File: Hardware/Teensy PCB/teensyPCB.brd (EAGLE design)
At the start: 100 x 50 mm, 9 parts, among them U1 HC_05, U2 USD-SOCKETNEW

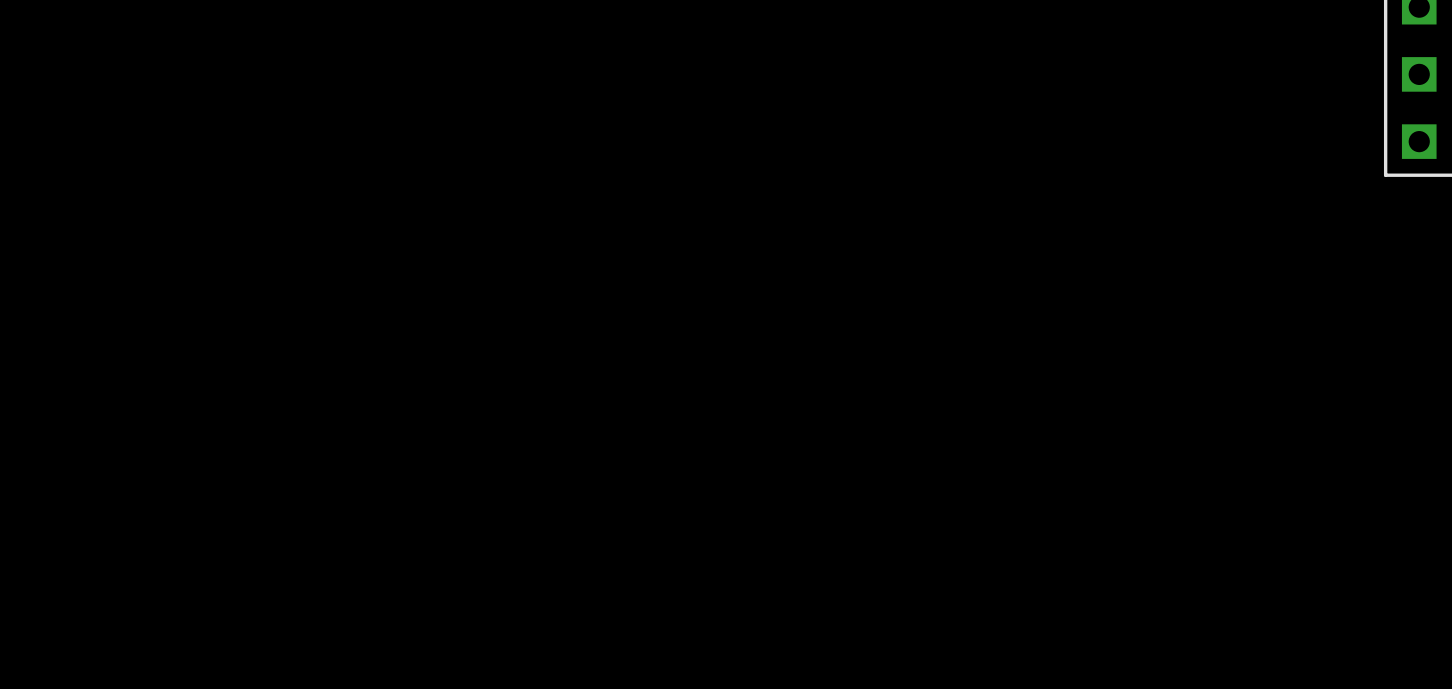
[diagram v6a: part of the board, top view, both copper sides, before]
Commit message: First attempt at wiring the audio (could be totally wrong)
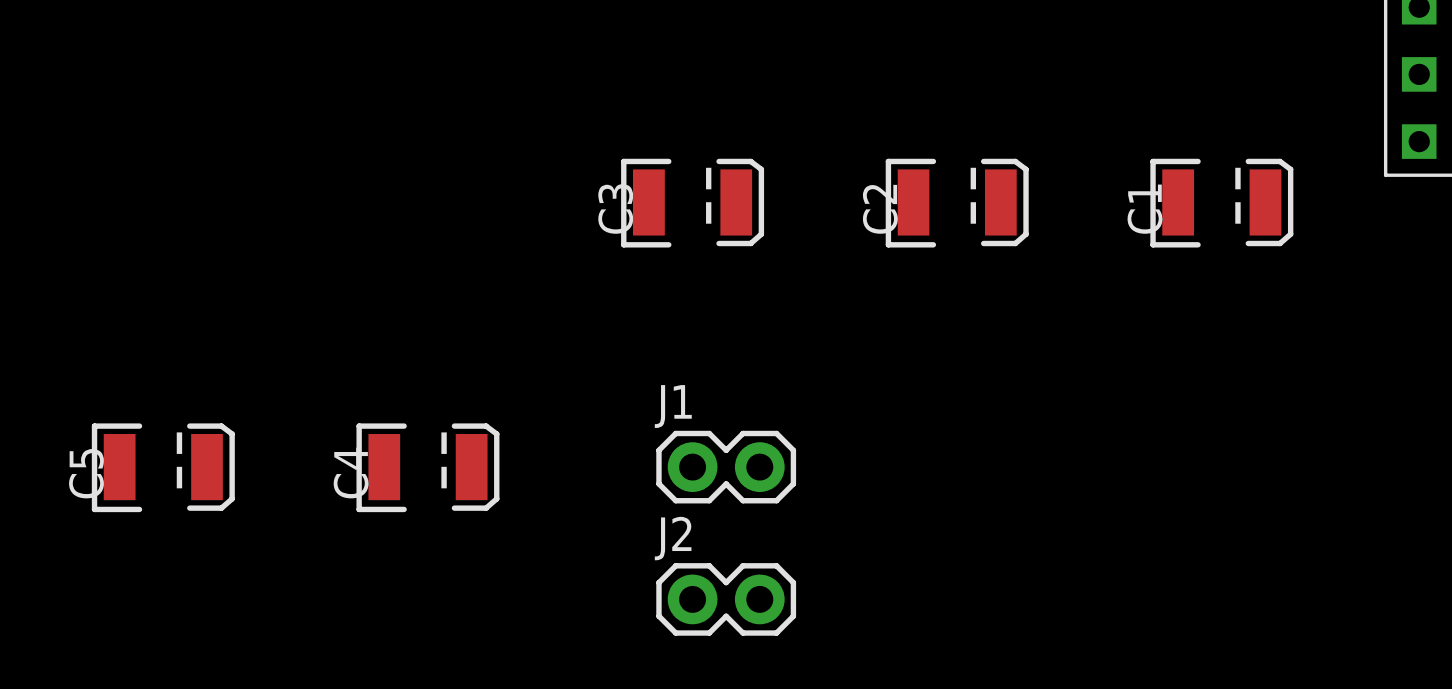
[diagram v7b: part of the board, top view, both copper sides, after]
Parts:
- added C1: 47uF, SparkFun-Capacitors:EIA3528
- added C2, C3: 10uF, SparkFun-Capacitors:EIA3528
- added C4, C5: 470uF, SparkFun-Capacitors:EIA3528
- added J1, J2: (no value), SparkFun-Connectors:1X02
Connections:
- new net DAC: C2.A, C3.A, U$1.RESET/DAC
- new net N$1: C2.C, U$4.LN
- new net N$2: C3.C, U$4.RN
- new net N$3: C4.C, J1.2
- new net N$4: C5.C, J2.2
- new net N$5: C4.A, U$4.R+
- new net N$6: J1.1, U$4.R-
- new net N$7: J2.1, U$4.L-
- new net N$8: C5.A, U$4.L+
- net 5V: now also C1.A
- net GND: now also C1.C
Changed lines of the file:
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@@
 <layer number="56" name="wert" color="7" fill="1" visible="yes" active="yes"/>
 <layer number="57" name="tCAD" color="7" fill="1" visible="no" active="no"/>
+<layer number="59" name="tCarbon" color="7" fill="1" visible="no" active="no"/>
+<layer number="60" name="bCarbon" color="7" fill="1" visible="no" active="no"/>
 <layer number="90" name="Modules" color="5" fill="1" visible="no" active="no"/>
 <layer number="91" name="Nets" color="2" fill="1" visible="no" active="no"/>
@@
 <layer number="112" name="tSilk" color="7" fill="1" visible="yes" active="yes"/>
 <layer number="113" name="IDFDebug" color="4" fill="1" visible="yes" active="yes"/>
+<layer number="114" name="Badge_Outline" color="7" fill="1" visible="yes" active="yes"/>
+<layer number="115" name="ReferenceISLANDS" color="7" fill="1" visible="yes" active="yes"/>
 <layer number="116" name="Patch_BOT" color="9" fill="4" visible="yes" active="yes"/>
+<layer number="118" name="Rect_Pads" color="7" fill="1" visible="yes" active="yes"/>
 <layer number="121" name="_tsilk" color="7" fill="1" visible="yes" active="yes"/>
 <layer number="122" name="_bsilk" color="7" fill="1" visible="yes" active="yes"/>
@@
 <layer number="127" name="_tValues" color="7" fill="1" visible="yes" active="yes"/>
 <layer number="128" name="_bValues" color="7" fill="1" visible="yes" active="yes"/>
+<layer number="129" name="Mask" color="7" fill="1" visible="yes" active="yes"/>
 <layer number="131" name="tAdjust" color="7" fill="1" visible="yes" active="yes"/>
 <layer number="132" name="bAdjust" color="7" fill="1" visible="yes" active="yes"/>
@@
 <layer number="223" name="223bmp" color="24" fill="1" visible="no" active="no"/>
 <layer number="224" name="224bmp" color="25" fill="1" visible="no" active="no"/>
+<layer number="225" name="225bmp" color="7" fill="1" visible="yes" active="yes"/>
+<layer number="226" name="226bmp" color="7" fill="1" visible="yes" active="yes"/>
+<layer number="227" name="227bmp" color="7" fill="1" visible="yes" active="yes"/>
+<layer number="228" name="228bmp" color="7" fill="1" visible="yes" active="yes"/>
+<layer number="229" name="229bmp" color="7" fill="1" visible="yes" active="yes"/>
+<layer number="230" name="230bmp" color="7" fill="1" visible="yes" active="yes"/>
+<layer number="231" name="231bmp" color="7" fill="1" visible="yes" active="yes"/>
 <layer number="248" name="Housing" color="7" fill="1" visible="yes" active="yes"/>
 <layer number="249" name="Edge" color="7" fill="1" visible="yes" active="yes"/>
@@
 <layer number="251" name="SMDround" color="12" fill="11" visible="no" active="no"/>
 <layer number="254" name="cooling" color="7" fill="1" visible="yes" active="yes"/>
+<layer number="255" name="routoute" color="7" fill="1" visible="yes" active="yes"/>
 </layers>
 <board>
@@
 <element name="U$3" library="IIC OLED MODULE LIBRARY" package="IIC128X64OLED" value="IIC128X64OLED" x="-120" y="10"/>
 <element name="U$4" library="CLASS D AUDIO AMP" package="AUDIOAMP" value="AUDIOAMP" x="-145" y="10"/>
+<element name="C1" library="SparkFun-Capacitors" package="EIA3528" value="47uF" x="-155" y="-5"/>
+<element name="C2" library="SparkFun-Capacitors" package="EIA3528" value="10uF" x="-165" y="-5"/>
+<element name="C3" library="SparkFun-Capacitors" package="EIA3528" value="10uF" x="-175" y="-5"/>
+<element name="J1" library="SparkFun-Connectors" package="1X02" value="" x="-175" y="-15"/>
+<element name="J2" library="SparkFun-Connectors" package="1X02" value="" x="-175" y="-20"/>
+<element name="C4" library="SparkFun-Capacitors" package="EIA3528" value="470uF" x="-185" y="-15"/>
+<element name="C5" library="SparkFun-Capacitors" package="EIA3528" value="470uF" x="-195" y="-15"/>
 </elements>
 <signals>
@@
 <contactref element="U$2" pad="GND"/>
 <contactref element="U$3" pad="GND"/>
+<contactref element="U$4" pad="GND2"/>
+<contactref element="U$4" pad="GND1"/>
+<contactref element="C1" pad="C"/>
 <contactref element="U$4" pad="GND0"/>
-<contactref element="U$4" pad="GND1"/>
-<contactref element="U$4" pad="GND2"/>
+<wire x1="-147.54" y1="-0.16" x2="-156.65" y2="-5" width="0" layer="19" extent="1-1"/>
 <wire x1="-147.54" y1="4.92" x2="-147.54" y2="-0.16" width="0" layer="19" extent="1-1"/>
 <wire x1="-147.54" y1="12.54" x2="-147.54" y2="4.92" width="0" layer="19" extent="1-1"/>
@@
 <contactref element="TOBALANCE" pad="6"/>
 <contactref element="U$4" pad="+5V"/>
+<contactref element="C1" pad="A"/>
+<wire x1="-147.54" y1="10" x2="-153.35" y2="-5" width="0" layer="19" extent="1-1"/>
 <wire x1="-57.3" y1="-5.254" x2="-147.54" y2="10" width="0" layer="19" extent="1-1"/>
 </signal>
@@
 <wire x1="57.54" y1="11.03" x2="-120" y2="22.7" width="0" layer="19" extent="1-1"/>
 </signal>
+<signal name="N$1">
+<contactref element="U$4" pad="LN"/>
+<contactref element="C2" pad="C"/>
+<wire x1="-147.54" y1="2.38" x2="-166.65" y2="-5" width="0" layer="19" extent="1-1"/>
+</signal>
+<signal name="N$2">
+<contactref element="U$4" pad="RN"/>
+<contactref element="C3" pad="C"/>
+<wire x1="-147.54" y1="-2.7" x2="-176.65" y2="-5" width="0" layer="19" extent="1-1"/>
+</signal>
+<signal name="DAC">
+<contactref element="U$1" pad="RESET/DAC"/>
+<contactref element="C2" pad="A"/>
+<contactref element="C3" pad="A"/>
+<wire x1="-163.35" y1="-5" x2="-173.35" y2="-5" width="0" layer="19" extent="1-1"/>
+<wire x1="60.08" y1="8.49" x2="-163.35" y2="-5" width="0" layer="19" extent="1-1"/>
+</signal>
+<signal name="N$3">
+<contactref element="J1" pad="2"/>
+<contactref element="C4" pad="C"/>
+<wire x1="-172.46" y1="-15" x2="-186.65" y2="-15" width="0" layer="19" extent="1-1"/>
+</signal>
+<signal name="N$4">
+<contactref element="J2" pad="2"/>
+<contactref element="C5" pad="C"/>
+<wire x1="-172.46" y1="-20" x2="-196.65" y2="-15" width="0" layer="19" extent="1-1"/>
+</signal>
+<signal name="N$5">
+<contactref element="C4" pad="A"/>
+<contactref element="U$4" pad="R+"/>
+<wire x1="-147.54" y1="22.7" x2="-183.35" y2="-15" width="0" layer="19" extent="1-1"/>
+</signal>
+<signal name="N$6">
+<contactref element="J1" pad="1"/>
+<contactref element="U$4" pad="R-"/>
+<wire x1="-147.54" y1="20.16" x2="-175" y2="-15" width="0" layer="19" extent="1-1"/>
+</signal>
+<signal name="N$7">
+<contactref element="U$4" pad="L-"/>
+<contactref element="J2" pad="1"/>
+<wire x1="-147.54" y1="15.08" x2="-175" y2="-20" width="0" layer="19" extent="1-1"/>
+</signal>
+<signal name="N$8">
+<contactref element="C5" pad="A"/>
+<contactref element="U$4" pad="L+"/>
+<wire x1="-147.54" y1="17.62" x2="-193.35" y2="-15" width="0" layer="19" extent="1-1"/>
+</signal>
 </signals>

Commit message: Modified audio connections
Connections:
- net N$3: now also C5.C, J2.1; no longer C4.C, J1.2
- net N$4: now also C4.C, J1.1; no longer C5.C, J2.2
- net N$6: now also J1.2; no longer J1.1
- net N$7: now also J2.2; no longer J2.1
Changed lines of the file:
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@@
 <wire x1="60.08" y1="8.49" x2="-163.35" y2="-5" width="0" layer="19" extent="1-1"/>
-</signal>
-<signal name="N$3">
-<contactref element="J1" pad="2"/>
-<contactref element="C4" pad="C"/>
-<wire x1="-172.46" y1="-15" x2="-186.65" y2="-15" width="0" layer="19" extent="1-1"/>
-</signal>
-<signal name="N$4">
-<contactref element="J2" pad="2"/>
-<contactref element="C5" pad="C"/>
-<wire x1="-172.46" y1="-20" x2="-196.65" y2="-15" width="0" layer="19" extent="1-1"/>
 </signal>
 <signal name="N$5">
@@
 </signal>
 <signal name="N$6">
-<contactref element="J1" pad="1"/>
 <contactref element="U$4" pad="R-"/>
-<wire x1="-147.54" y1="20.16" x2="-175" y2="-15" width="0" layer="19" extent="1-1"/>
+<contactref element="J1" pad="2"/>
+<wire x1="-147.54" y1="20.16" x2="-172.46" y2="-15" width="0" layer="19" extent="1-1"/>
 </signal>
 <signal name="N$7">
 <contactref element="U$4" pad="L-"/>
-<contactref element="J2" pad="1"/>
-<wire x1="-147.54" y1="15.08" x2="-175" y2="-20" width="0" layer="19" extent="1-1"/>
+<contactref element="J2" pad="2"/>
+<wire x1="-147.54" y1="15.08" x2="-172.46" y2="-20" width="0" layer="19" extent="1-1"/>
 </signal>
 <signal name="N$8">
@@
 <wire x1="-147.54" y1="17.62" x2="-193.35" y2="-15" width="0" layer="19" extent="1-1"/>
 </signal>
+<signal name="N$3">
+<contactref element="C5" pad="C"/>
+<contactref element="J2" pad="1"/>
+<wire x1="-175" y1="-20" x2="-196.65" y2="-15" width="0" layer="19" extent="1-1"/>
+</signal>
+<signal name="N$4">
+<contactref element="C4" pad="C"/>
+<contactref element="J1" pad="1"/>
+<wire x1="-175" y1="-15" x2="-186.65" y2="-15" width="0" layer="19" extent="1-1"/>
+</signal>
 </signals>
